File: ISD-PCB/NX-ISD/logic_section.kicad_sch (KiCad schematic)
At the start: 10 parts, among them J1 1-2328702-0, Q4 AO3400A, U1 ESP32-S3-WROOM-1, U14 ZDSD02GLGEAG

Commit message: Updated v1p0 files
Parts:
- added C16: 10u, Capacitor_SMD:C_0603_1608Metric, symbol Device:C
- added C17: 100n, Capacitor_SMD:C_0402_1005Metric, symbol Device:C
- C8: value 1uF -> 1u
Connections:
- net +3V3: now also C16.1, C17.1
- net GND: now also C16.2, C17.2

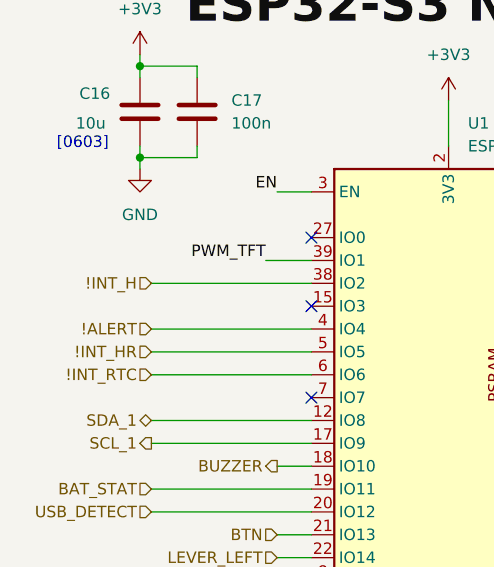
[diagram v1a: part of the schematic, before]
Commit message: updated labels
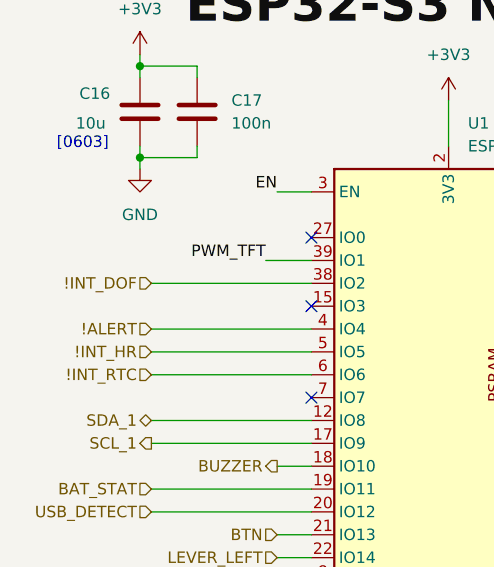
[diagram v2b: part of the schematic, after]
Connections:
- net !INT_H renamed !INT_DOF
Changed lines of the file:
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@@
 		)
 	)
-	(hierarchical_label "!INT_H"
+	(hierarchical_label "!INT_DOF"
 		(shape input)
 		(at 29.21 53.34 180)

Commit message: Fixed: polarity of NPM Pmos
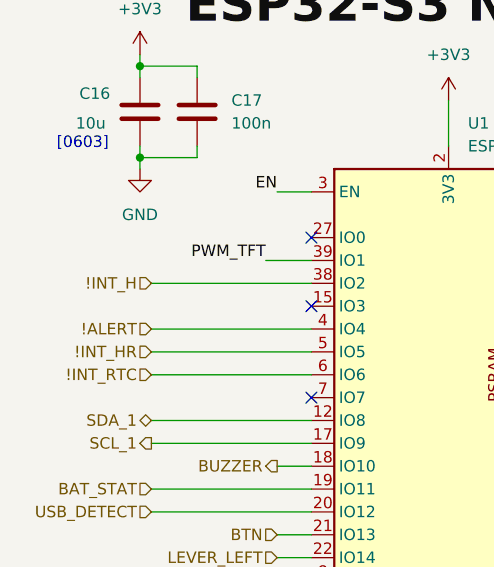
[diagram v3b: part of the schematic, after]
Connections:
- net !INT_DOF renamed !INT_H
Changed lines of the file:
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@@
 		)
 	)
-	(hierarchical_label "!INT_DOF"
+	(hierarchical_label "!INT_H"
 		(shape input)
 		(at 29.21 53.34 180)

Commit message: v1p1 rework in progress
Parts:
- removed J1: 1-2328702-0, Global Footprints:TE_1-2328702-0, symbol 1-2328702-0:1-2328702-0
- removed Q4: AO3400A, Package_TO_SOT_SMD:SOT-23, symbol Transistor_FET:AO3400A
- removed R10, R15: 220, Resistor_SMD:R_0402_1005Metric, symbol Device:R
- removed R14: 10k, Resistor_SMD:R_0402_1005Metric, symbol Device:R
- removed U14: ZDSD02GLGEAG, Global Footprints:LGA-8_L8.0-W6.0-P1.27-TL_ZDSD02GLGEAG, symbol ZDSD02GLGEAG:ZDSD02GLGEAG
- added JP3: BOOT, Jumper:SolderJumper-2_P1.3mm_Open_TrianglePad1.0x1.5mm, symbol Jumper:SolderJumper_2_Open
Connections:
- net GND: now also JP3.2 (B)
- net BOOT: now reaches U1.27 (IO0)
- net BOOT: now also JP3.1 (A)
- net RS renamed DC
- no-connect marks 12 -> 9
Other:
- moved on the sheet: C16, C17, C8, JP2, R3, U1

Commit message: v1p3 - Isssues fixed
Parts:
- U13: renamed from U1; value ESP32-S3-WROOM-1 -> ESP32-S3-WROOM-1_N16R8
- renumbered C16 to C24, C17 to C25, C8 to C26, R3 to R19
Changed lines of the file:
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@@
 	(wire
 		(pts
-			(xy 52.07 50.8) (xy 55.88 50.8)
+			(xy 50.8 50.8) (xy 55.88 50.8)
 		)
 		(stroke
@@
 	(wire
 		(pts
-			(xy 52.07 45.72) (xy 55.88 45.72)
+			(xy 50.8 45.72) (xy 55.88 45.72)
 		)
 		(stroke
@@
 	)
 	(label "EN"
-		(at 52.07 45.72 180)
+		(at 50.8 45.72 180)
 		(effects
 			(font
@@
 	)
 	(label "BOOT"
-		(at 52.07 50.8 180)
+		(at 50.8 50.8 180)
 		(effects
 			(font
@@
 		(dnp no)
 		(fields_autoplaced yes)
-		(property "Reference" "#PWR0136"
+		(property "Reference" "#PWR091"
 			(at 171.45 74.93 0)
 			(hide yes)
@@
 			(project "NX-ISD"
 				(path "/3830a648-69ee-45ab-8814-deeba52753c2/585f3487-1bfc-48d8-9703-af93405d2d15"
-					(reference "#PWR0136")
+					(reference "#PWR091")
 					(unit 1)
 				)
@@
 		(dnp no)
 		(fields_autoplaced yes)
-		(property "Reference" "#PWR01"
+		(property "Reference" "#PWR087"
 			(at 71.12 106.68 0)
 			(hide yes)
@@
 			(project "NX-ISD"
 				(path "/3830a648-69ee-45ab-8814-deeba52753c2/585f3487-1bfc-48d8-9703-af93405d2d15"
-					(reference "#PWR01")
+					(reference "#PWR087")
 					(unit 1)
 				)
@@
 		(dnp no)
 		(fields_autoplaced yes)
-		(property "Reference" "#PWR0116"
+		(property "Reference" "#PWR085"
 			(at 36.83 128.27 0)
 			(hide yes)
@@
 			(project "NX-ISD"
 				(path "/3830a648-69ee-45ab-8814-deeba52753c2/585f3487-1bfc-48d8-9703-af93405d2d15"
-					(reference "#PWR0116")
+					(reference "#PWR085")
 					(unit 1)
 				)
@@
 		(dnp no)
 		(fields_autoplaced yes)
-		(property "Reference" "#PWR0112"
+		(property "Reference" "#PWR088"
 			(at 140.97 74.93 0)
 			(hide yes)
@@
 			(project "NX-ISD"
 				(path "/3830a648-69ee-45ab-8814-deeba52753c2/585f3487-1bfc-48d8-9703-af93405d2d15"
-					(reference "#PWR0112")
+					(reference "#PWR088")
 					(unit 1)
 				)
@@
 		(dnp no)
 		(fields_autoplaced yes)
-		(property "Reference" "C17"
+		(property "Reference" "C25"
 			(at 46.99 114.2999 0)
 			(show_name no)
@@
 			(project "NX-ISD"
 				(path "/3830a648-69ee-45ab-8814-deeba52753c2/585f3487-1bfc-48d8-9703-af93405d2d15"
-					(reference "C17")
+					(reference "C25")
 					(unit 1)
 				)
@@
 		(dnp no)
 		(fields_autoplaced yes)
-		(property "Reference" "R3"
+		(property "Reference" "R19"
 			(at 149.86 49.5299 0)
 			(show_name no)
@@
 			(project "NX-ISD"
 				(path "/3830a648-69ee-45ab-8814-deeba52753c2/585f3487-1bfc-48d8-9703-af93405d2d15"
-					(reference "R3")
+					(reference "R19")
 					(unit 1)
 				)
@@
 		(in_pos_files yes)
 		(dnp no)
-		(property "Reference" "C16"
+		(property "Reference" "C24"
 			(at 33.528 113.538 0)
 			(show_name no)
@@
 			(project "NX-ISD"
 				(path "/3830a648-69ee-45ab-8814-deeba52753c2/585f3487-1bfc-48d8-9703-af93405d2d15"
-					(reference "C16")
+					(reference "C24")
 					(unit 1)
 				)
@@
 		(dnp no)
 		(fields_autoplaced yes)
-		(property "Reference" "#PWR02"
+		(property "Reference" "#PWR086"
 			(at 71.12 39.37 0)
 			(hide yes)
@@
 			(project "NX-ISD"
 				(path "/3830a648-69ee-45ab-8814-deeba52753c2/585f3487-1bfc-48d8-9703-af93405d2d15"
-					(reference "#PWR02")
+					(reference "#PWR086")
 					(unit 1)
 				)
@@
 		(in_pos_files yes)
 		(dnp no)
-		(property "Reference" "C8"
+		(property "Reference" "C26"
 			(at 150.622 58.928 0)
 			(show_name no)
@@
 			(project "NX-ISD"
 				(path "/3830a648-69ee-45ab-8814-deeba52753c2/585f3487-1bfc-48d8-9703-af93405d2d15"
-					(reference "C8")
+					(reference "C26")
 					(unit 1)
 				)
@@
 		(dnp no)
 		(fields_autoplaced yes)
-		(property "Reference" "#PWR033"
+		(property "Reference" "#PWR090"
 			(at 147.32 74.93 0)
 			(hide yes)
@@
 			(project "NX-ISD"
 				(path "/3830a648-69ee-45ab-8814-deeba52753c2/585f3487-1bfc-48d8-9703-af93405d2d15"
-					(reference "#PWR033")
+					(reference "#PWR090")
 					(unit 1)
 				)
@@
 		(dnp no)
 		(fields_autoplaced yes)
-		(property "Reference" "U1"
+		(property "Reference" "U13"
 			(at 73.2633 38.1 0)
 			(show_name no)
@@
 			)
 		)
-		(property "Value" "ESP32-S3-WROOM-1"
+		(property "Value" "ESP32-S3-WROOM-1_N16R8"
 			(at 73.2633 40.64 0)
 			(show_name no)
@@
 			(project "NX-ISD"
 				(path "/3830a648-69ee-45ab-8814-deeba52753c2/585f3487-1bfc-48d8-9703-af93405d2d15"
-					(reference "U1")
+					(reference "U13")
 					(unit 1)
 				)
@@
 		(dnp no)
 		(fields_autoplaced yes)
-		(property "Reference" "#PWR034"
+		(property "Reference" "#PWR089"
 			(at 147.32 46.99 0)
 			(hide yes)
@@
 			(project "NX-ISD"
 				(path "/3830a648-69ee-45ab-8814-deeba52753c2/585f3487-1bfc-48d8-9703-af93405d2d15"
-					(reference "#PWR034")
+					(reference "#PWR089")
 					(unit 1)
 				)
@@
 		(dnp no)
 		(fields_autoplaced yes)
-		(property "Reference" "#PWR0115"
+		(property "Reference" "#PWR084"
 			(at 36.83 113.03 0)
 			(hide yes)
@@
 			(project "NX-ISD"
 				(path "/3830a648-69ee-45ab-8814-deeba52753c2/585f3487-1bfc-48d8-9703-af93405d2d15"
-					(reference "#PWR0115")
+					(reference "#PWR084")
 					(unit 1)
 				)

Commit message: v1p3 - HRM Cap fix &more
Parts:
- U13: value ESP32-S3-WROOM-1_N16R8 -> ESP32-S3-WROOM-1-N16R8; MPN (none) -> ESP32-S3-WROOM-1-N16R8
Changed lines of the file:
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@@
 			)
 		)
-		(property "Value" "ESP32-S3-WROOM-1_N16R8"
+		(property "Value" "ESP32-S3-WROOM-1-N16R8"
 			(at 73.2633 40.64 0)
 			(show_name no)
@@
 			(at 71.12 68.58 0)
 			(hide yes)
+			(show_name no)
+			(do_not_autoplace no)
+			(effects
+				(font
+					(size 1.27 1.27)
+				)
+			)
+		)
+		(property "MPN" "ESP32-S3-WROOM-1-N16R8"
+			(at 71.12 68.58 0)
+			(hide yes)
